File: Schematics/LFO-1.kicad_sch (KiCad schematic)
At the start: 54 parts, among them J57 Conn_01x10h, J58 Conn_01x03, J59 Conn_01x04, J60 Conn_01x04, U101 LM324, U102 LM78L05, U103 SSI2130, U104 LM324, U105 LM324

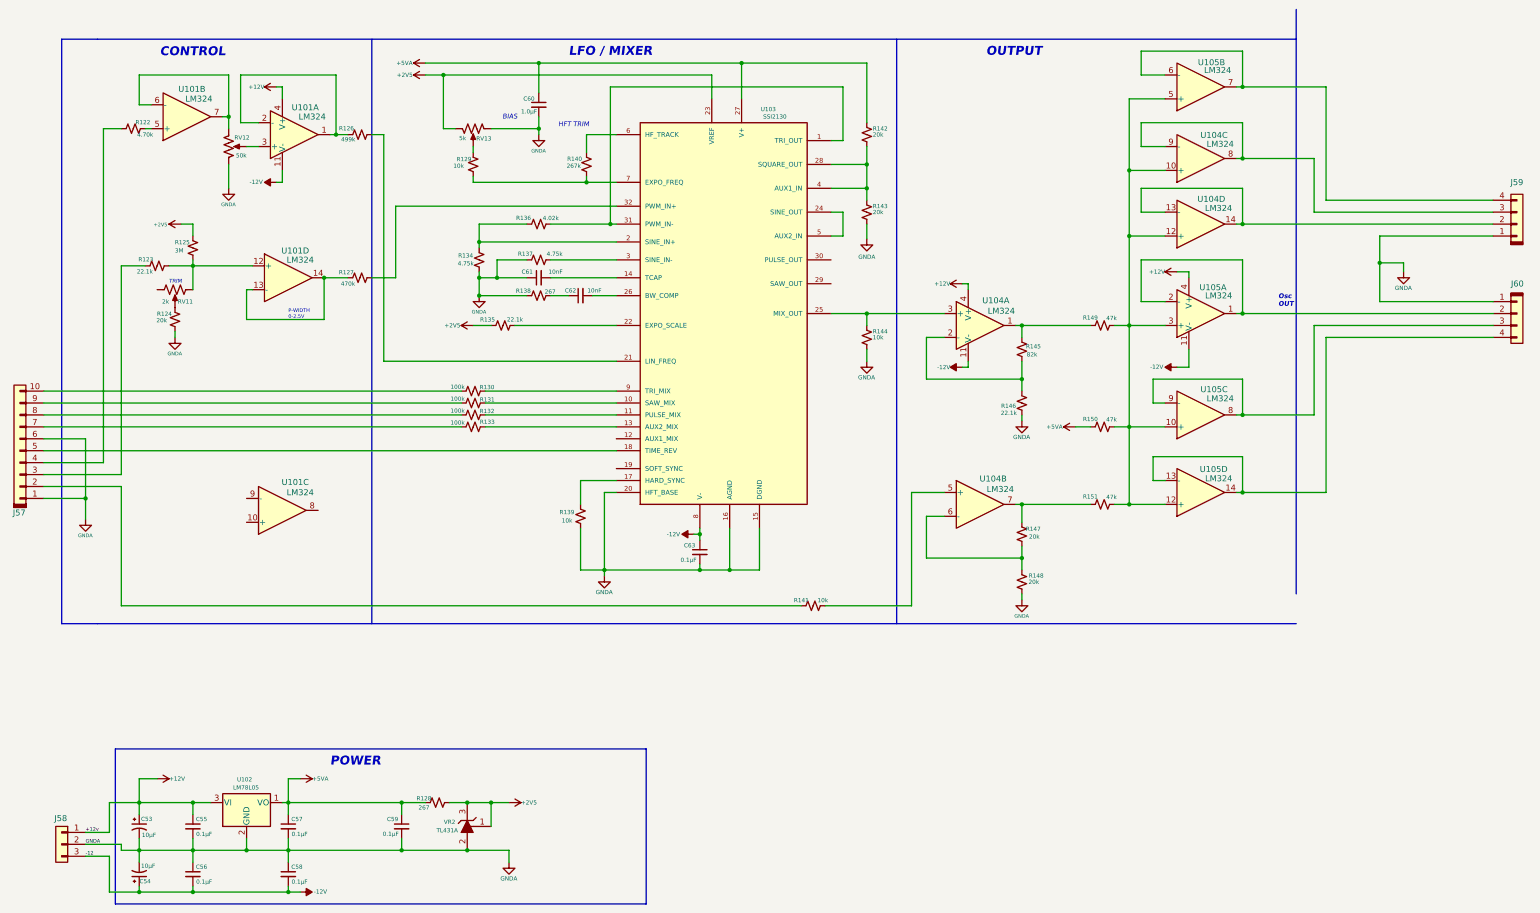
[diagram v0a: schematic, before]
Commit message: Now with dual ESP32 with Midi32 and Disp32.
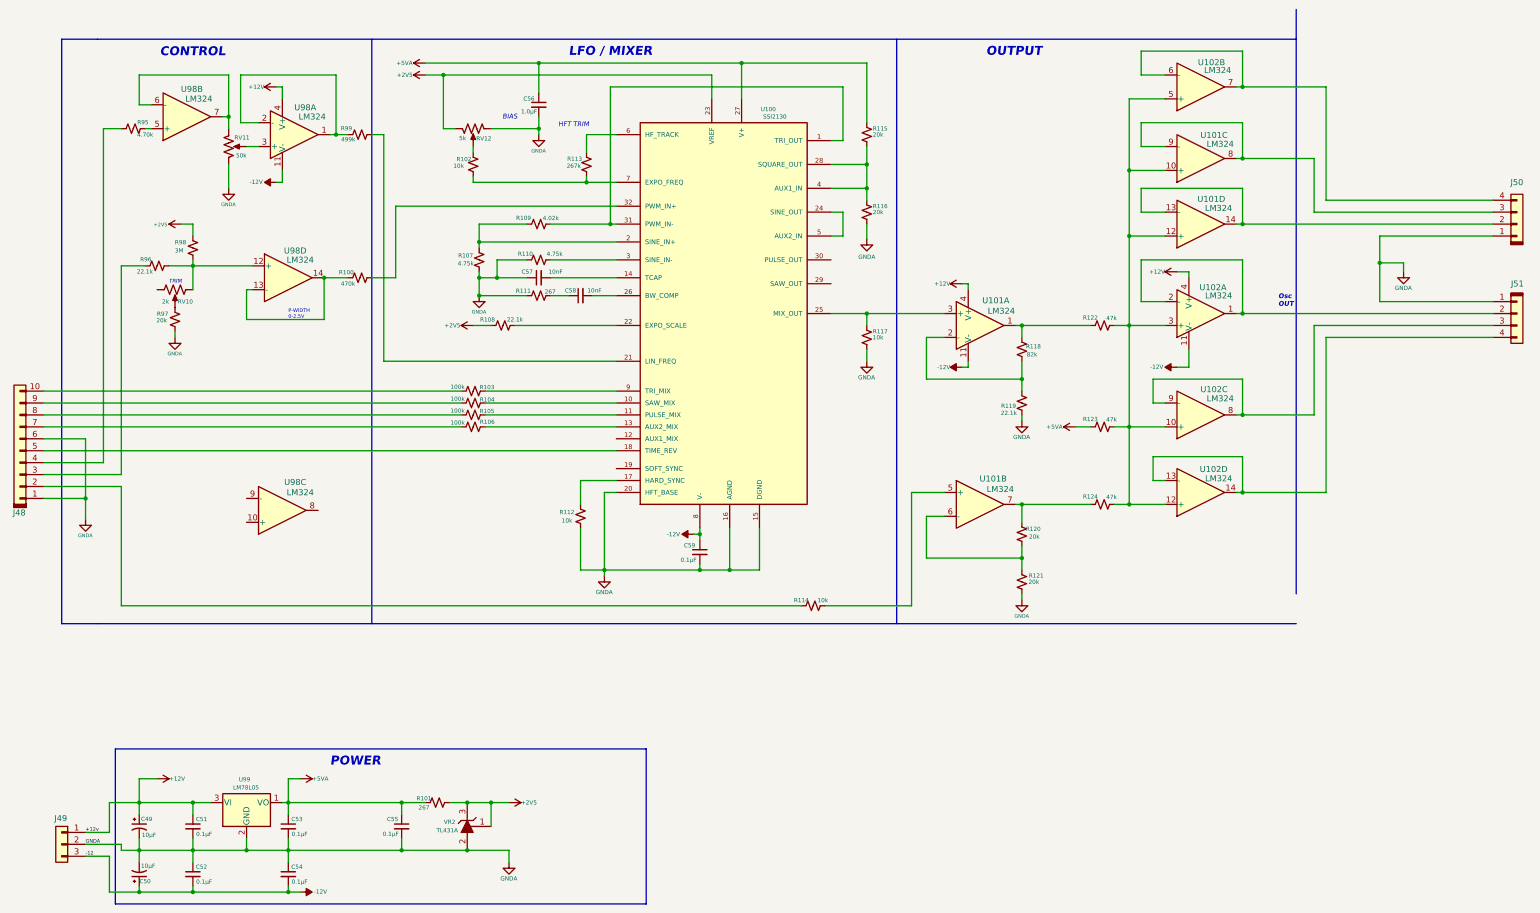
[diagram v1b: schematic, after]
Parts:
- renumbered C53 to C49, C54 to C50, C55 to C51, C56 to C52, C57 to C53, C58 to C54, C59 to C55, C60 to C56, C61 to C57, C62 to C58, C63 to C59, J57 to J48, J58 to J49, J59 to J50, J60 to J51, R127 to R100, R128 to R101, R129 to R102, R130 to R103, R131 to R104, R132 to R105, R133 to R106, R134 to R107, R135 to R108, R136 to R109, R137 to R110, R138 to R111, R139 to R112, R140 to R113, R141 to R114, R142 to R115, R143 to R116, R144 to R117, R145 to R118, R146 to R119, R147 to R120, R148 to R121, R149 to R122, R150 to R123, R151 to R124, R122 to R95, R123 to R96, R124 to R97, R125 to R98, R126 to R99, RV11 to RV10, RV12 to RV11, RV13 to RV12, U103 to U100, U104 to U101, U105 to U102, U101 to U98, U102 to U99
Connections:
- net at RV10. (3): now also R97.1

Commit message: Disp32 interface working properly.
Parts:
- renumbered J48 to J49, J49 to J50, J50 to J51, J51 to J52, R101 to R100, R102 to R101, R103 to R102, R104 to R103, R105 to R104, R106 to R105, R107 to R106, R108 to R107, R109 to R108, R110 to R109, R111 to R110, R112 to R111, R113 to R112, R114 to R113, R115 to R114, R116 to R115, R117 to R116, R118 to R117, R119 to R118, R120 to R119, R121 to R120, R122 to R121, R123 to R122, R124 to R123, R95 to R94, R96 to R95, R97 to R96, R98 to R97, R99 to R98, R100 to R99
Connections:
- net at RV10. (3): now also R96.1

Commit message: Noise generator and experimental steups.
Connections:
- net at RV10. (3): now also R96.1

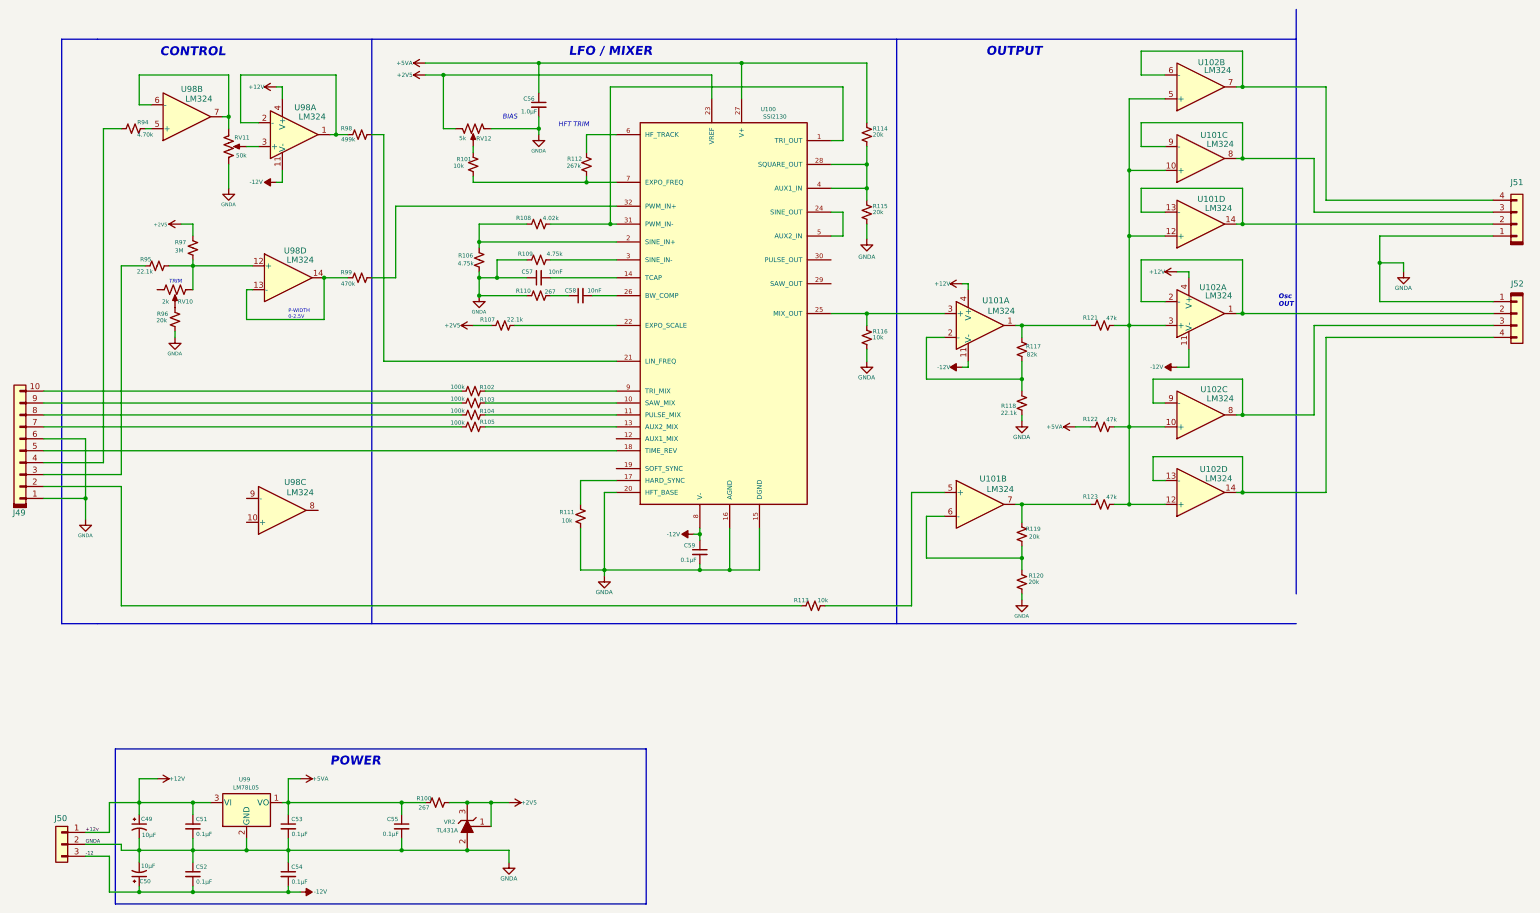
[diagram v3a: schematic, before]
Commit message: adding noise source and variable state filter.
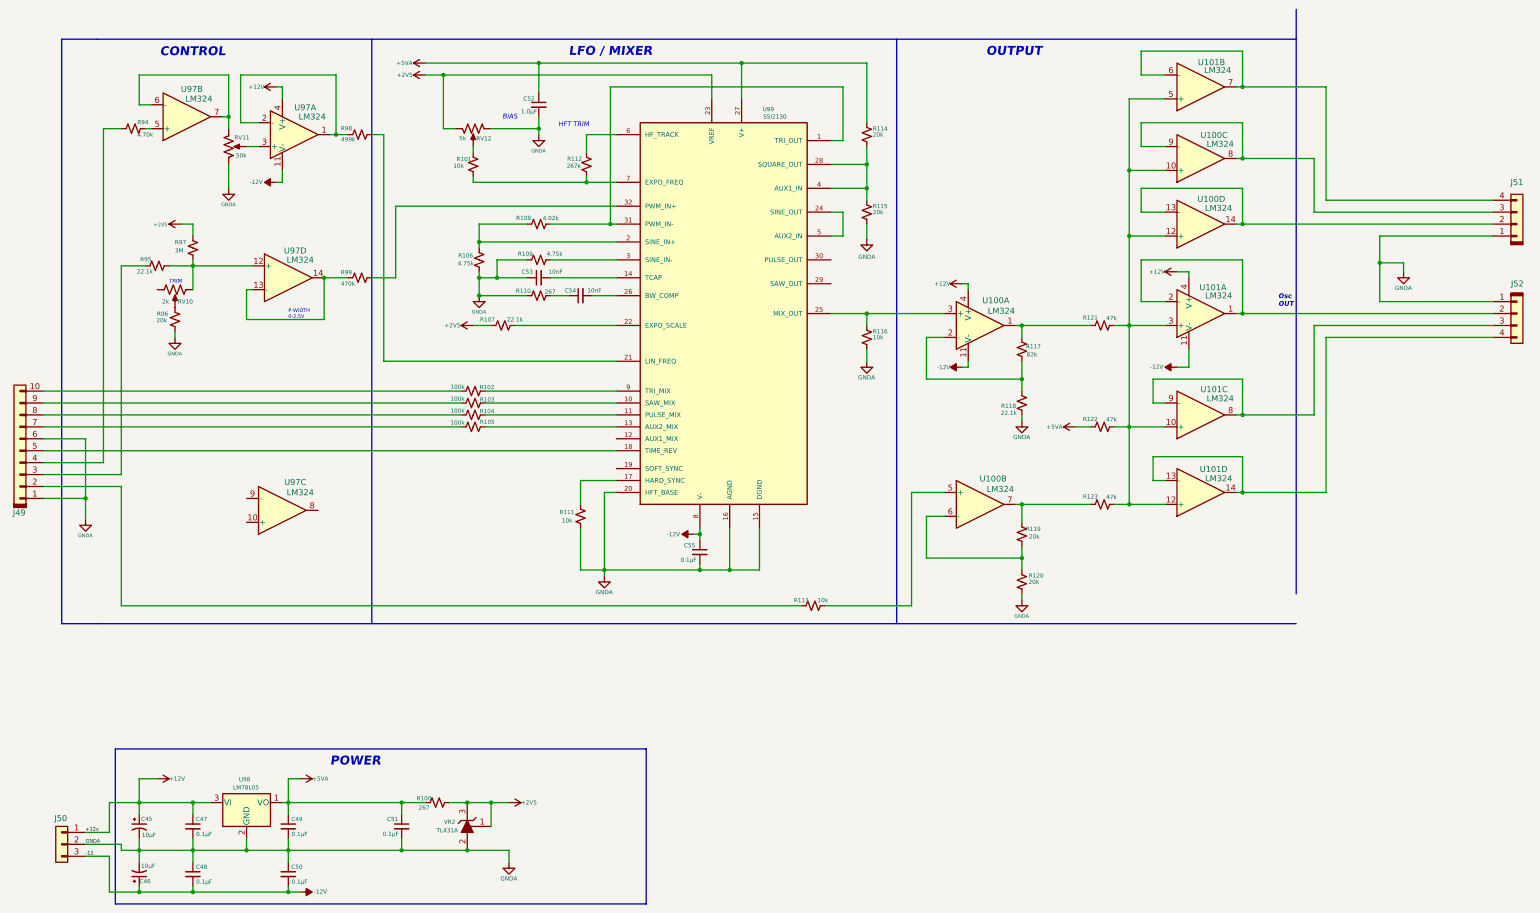
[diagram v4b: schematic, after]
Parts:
- renumbered C49 to C45, C50 to C46, C51 to C47, C52 to C48, C53 to C49, C54 to C50, C55 to C51, C56 to C52, C57 to C53, C58 to C54, C59 to C55, U101 to U100, U102 to U101, U98 to U97, U99 to U98, U100 to U99
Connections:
- net at RV10. (3): now also R96.1

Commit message: Noise boards added.
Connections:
- net at RV10. (3): now also R96.1

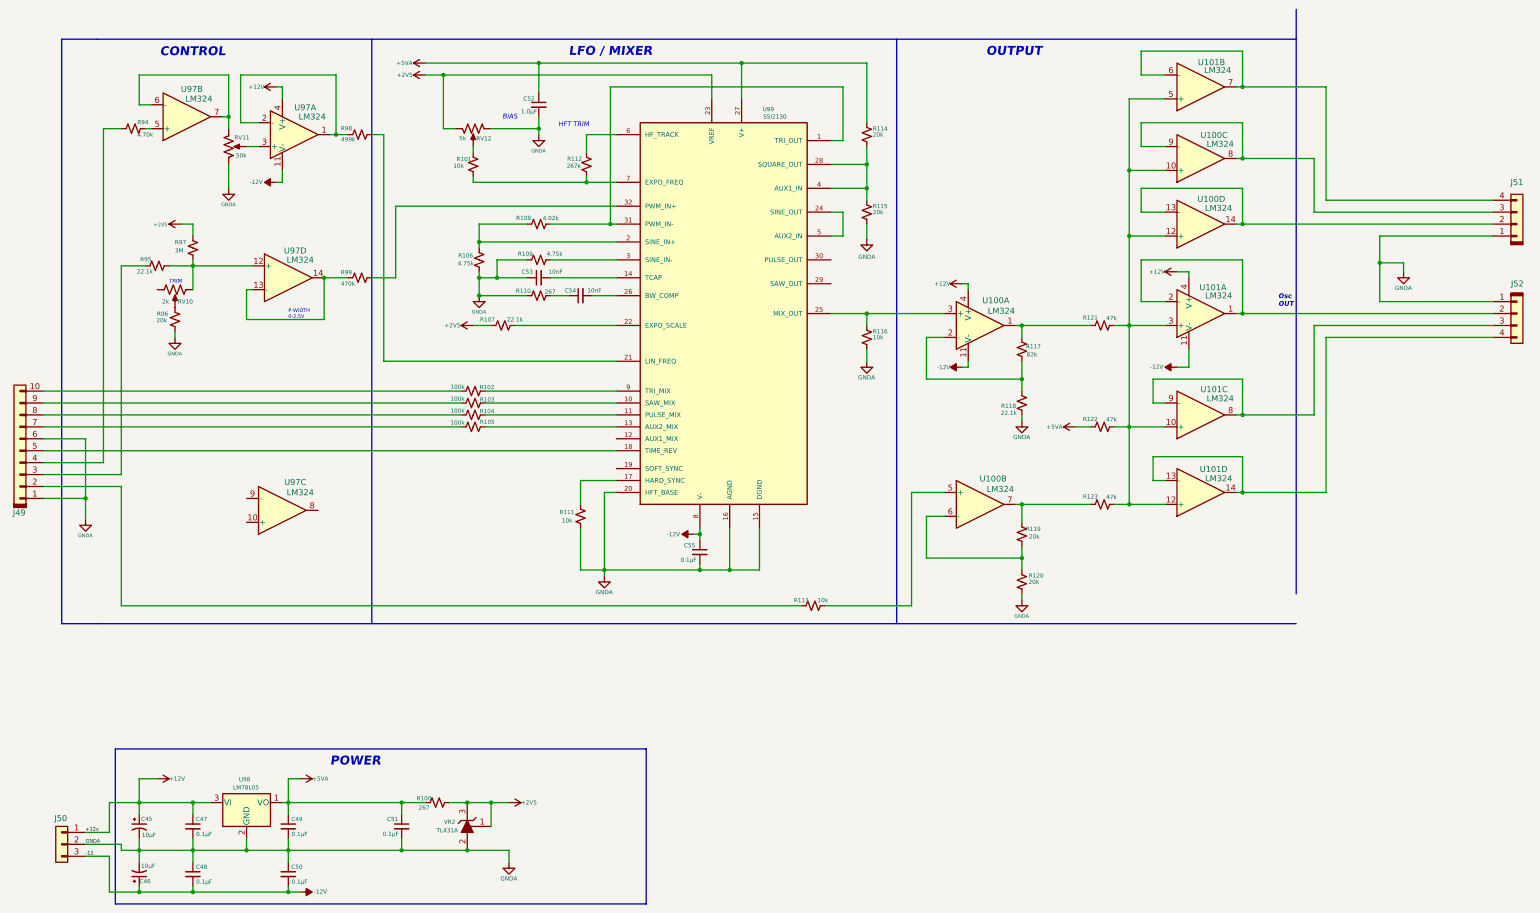
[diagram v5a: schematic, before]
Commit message: Update with noise filter & VCA as well as envelope generator software shell.
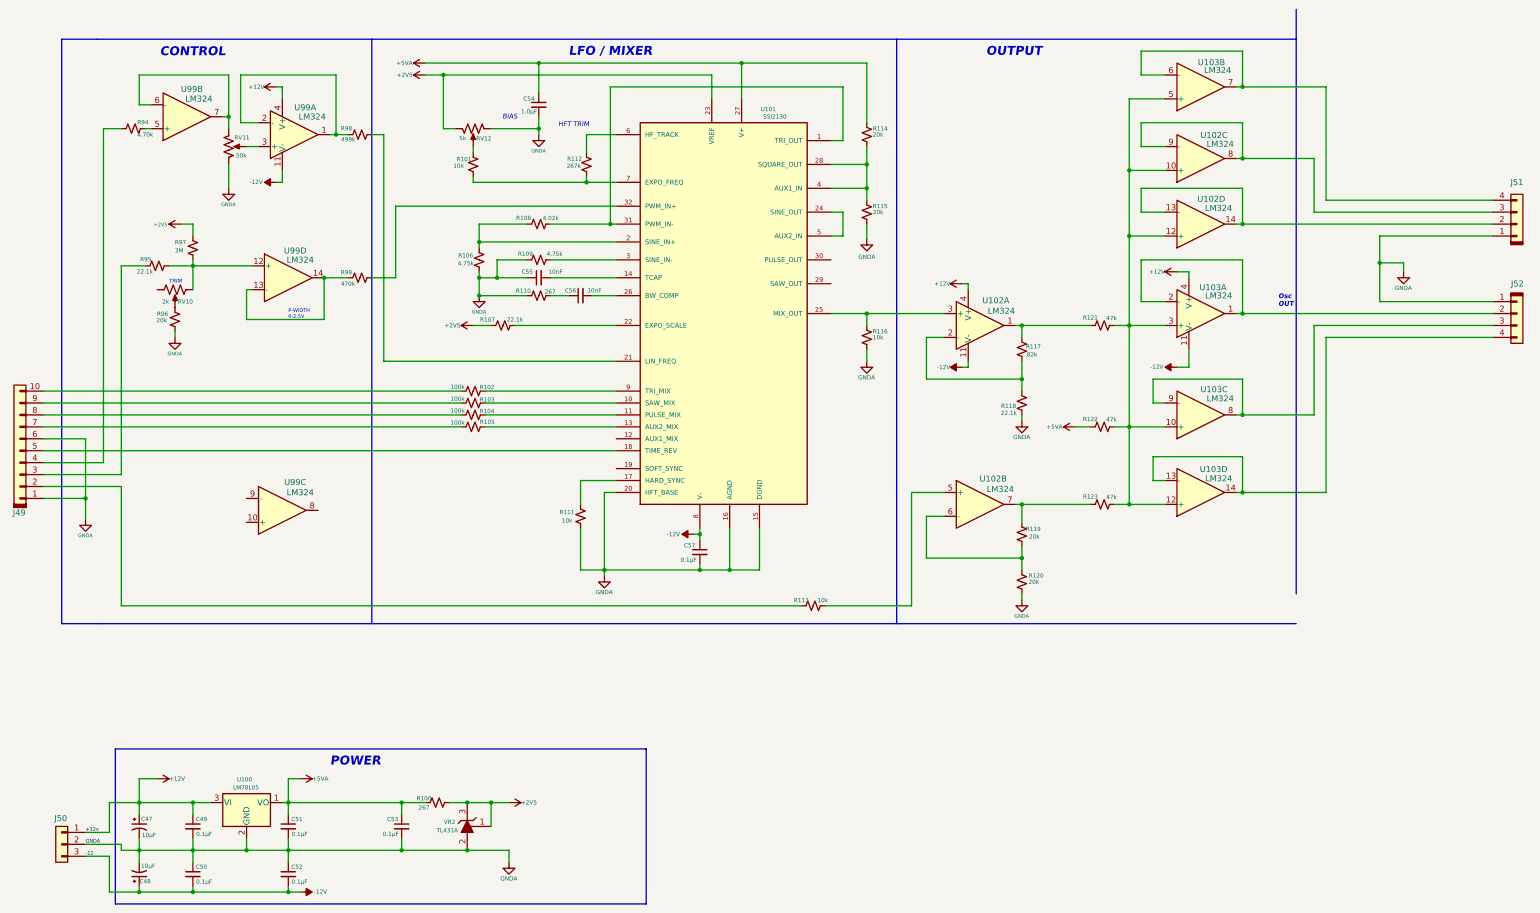
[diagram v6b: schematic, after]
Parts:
- renumbered C45 to C47, C46 to C48, C47 to C49, C48 to C50, C49 to C51, C50 to C52, C51 to C53, C52 to C54, C53 to C55, C54 to C56, C55 to C57, U98 to U100, U99 to U101, U100 to U102, U101 to U103, U97 to U99
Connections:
- net at RV10. (3): now also R96.1

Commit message: sync up first noise board.
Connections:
- net at RV10. (3): now also R96.1
